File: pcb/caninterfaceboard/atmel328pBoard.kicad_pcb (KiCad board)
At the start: 2 copper layers, 97.2 x 50.5 mm, 74 parts, among them J1 UART, J10 NTC2, J12 Flywheel, J13 1Wire, J2 NMEA2000, J3 AVR ISP, J4 NTC3, J5 NTC4, J6 FuelLevel, J7 Engine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

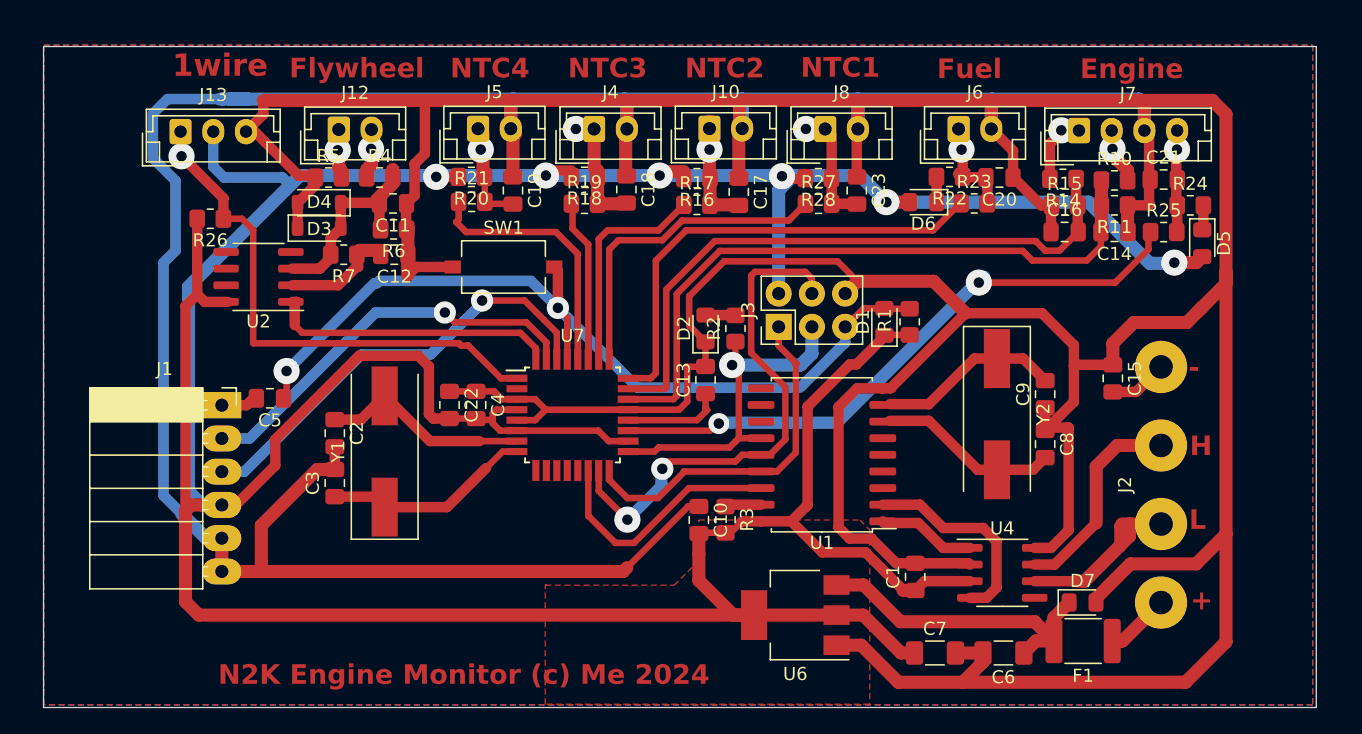
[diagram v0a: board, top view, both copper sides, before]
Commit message: Added oil pressure and status, modified pcb
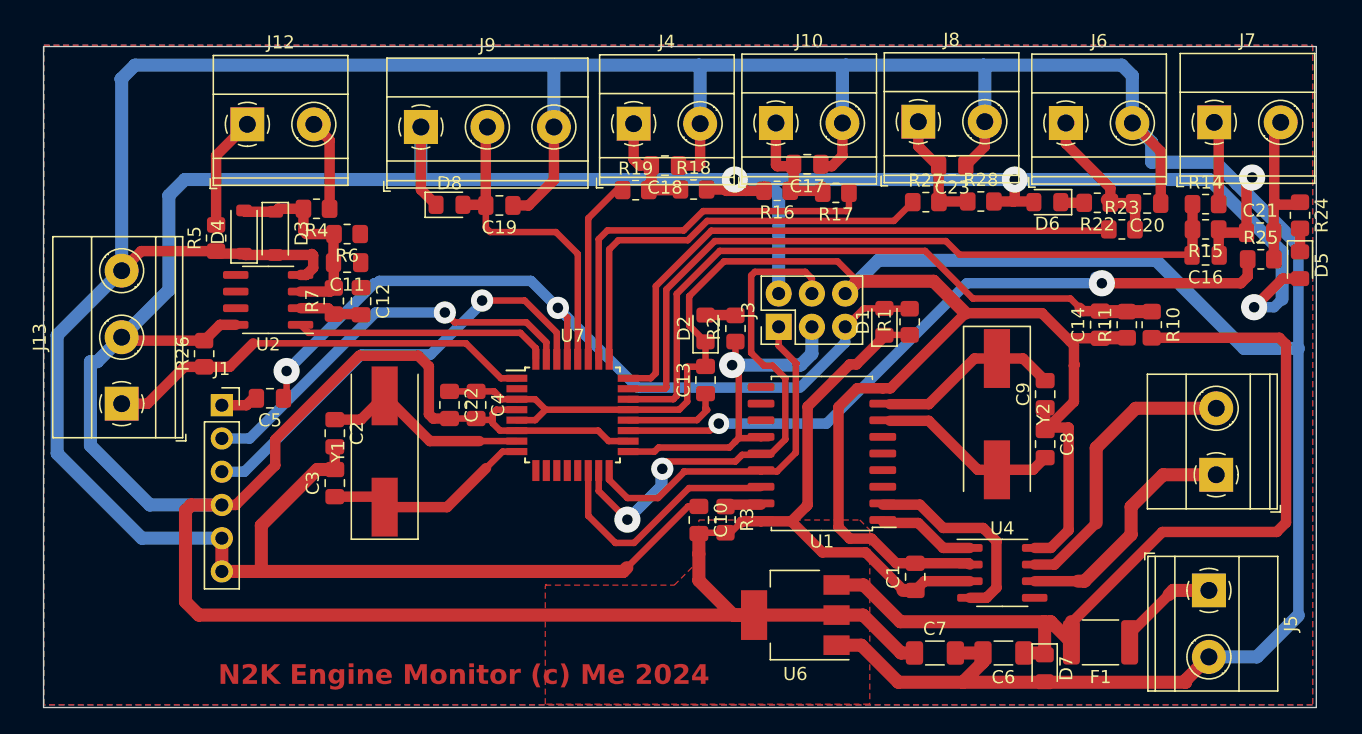
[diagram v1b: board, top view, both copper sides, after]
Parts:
- removed C15: 1uF, Capacitor_SMD:C_0805_2012Metric_Pad1.18x1.45mm_HandSolder
- removed R20: 4.7K, Resistor_SMD:R_0805_2012Metric_Pad1.20x1.40mm_HandSolder
- removed R21: 100K, Resistor_SMD:R_0805_2012Metric_Pad1.20x1.40mm_HandSolder
- removed SW1: Reset, Button_Switch_SMD:SW_Tactile_SPST_NO_Straight_CK_PTS636Sx25SMTRLFS
- added D8: S1J, Diode_SMD:D_0805_2012Metric_Pad1.15x1.40mm_HandSolder, F.Cu at (138.7, 62.7)
- added J9: Oil Pressure, TerminalBlock_Phoenix:TerminalBlock_Phoenix_MKDS-1,5-3-5.08_1x03_P5.08mm_Horizontal, F.Cu at (136.5, 56.7)
- J1: footprint Connector_PinSocket_2.54mm:PinSocket_1x06_P2.54mm_Horizontal -> Connector_PinSocket_2.54mm:PinSocket_1x06_P2.54mm_Vertical
- J10, J12, J4, J6, J8: footprint Connector_JST:JST_EH_B2B-EH-A_1x02_P2.50mm_Vertical -> TerminalBlock_Phoenix:TerminalBlock_Phoenix_MKDS-1,5-2-5.08_1x02_P5.08mm_Horizontal
- J13: footprint Connector_JST:JST_EH_B3B-EH-A_1x03_P2.50mm_Vertical -> TerminalBlock_Phoenix:TerminalBlock_Phoenix_MKDS-1,5-3-5.08_1x03_P5.08mm_Horizontal
- J2: value NMEA2000 -> CAN; footprint Connector_Wire:SolderWire-1.5sqmm_1x04_P6mm_D1.7mm_OD3mm -> TerminalBlock_Phoenix:TerminalBlock_Phoenix_MKDS-1,5-2-5.08_1x02_P5.08mm_Horizontal
- J5: value NTC4 -> 12V In; footprint Connector_JST:JST_EH_B2B-EH-A_1x02_P2.50mm_Vertical -> TerminalBlock_Phoenix:TerminalBlock_Phoenix_MKDS-1,5-2-5.08_1x02_P5.08mm_Horizontal
- J7: footprint Connector_JST:JST_EH_B4B-EH-A_1x04_P2.50mm_Vertical -> TerminalBlock_Phoenix:TerminalBlock_Phoenix_MKDS-1,5-2-5.08_1x02_P5.08mm_Horizontal
- moved J5 66.0 mm to (196.7, 92.1), turned to -90 degrees
- moved J13 21.3 mm to (113.6, 77.9), turned to 90 degrees
- moved R28 12.5 mm to (179.3, 62.4), turned to 0 degrees
- moved R23 11.5 mm to (190.0, 64.6)
- moved C20 11.5 mm to (192.0, 62.6)
- moved R22 11.5 mm to (188.2, 62.5)
- moved R10 11.4 mm to (192.3, 71.8), turned to -90 degrees
- moved R14 11.1 mm to (196.4, 62.6), turned to 0 degrees
- moved R15 10.9 mm to (196.4, 64.6), turned to 180 degrees
- moved C16 10.9 mm to (196.4, 66.5), turned to 180 degrees
- moved R17 10.7 mm to (168.2, 61.8), turned to 180 degrees
- moved J2 10.6 mm to (197.3, 83.3)
- moved J7 10.4 mm to (197.1, 56.4)
- moved R26 10.3 mm to (119.9, 74.1), turned to 90 degrees
- moved R5 9.75 mm to (120.9, 65.2), turned to 90 degrees
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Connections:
- C19 pad 2: Net-(J5-Pin_1) -> A5
- C6 pad 1: Net-(D7-K) -> Engine Batt+
- D7 pad 1: Net-(D7-K) -> Engine Batt+
- F1 pad 2: Net-(D7-K) -> Engine Batt+
- J2 pad 1: 12V -> CANHL
- J2 pad 2: CANHL -> CANH
- J5 pad 1: Net-(J5-Pin_1) -> 12V
- J7 pad 2: Engine Batt+ -> Coolant
- U6 pad 3: Net-(D7-K) -> Engine Batt+
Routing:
- net Engine Batt+: track 5.63 -> 70.7 mm, vias 1 -> 0
- net Engine Block: track 563.3 -> 508.9 mm, vias 0 -> 1
- net Net-(D7-K): track 24.5 -> 0.00 mm
- net A6: track 72.2 -> 54.4 mm
- net 5V: track 320.8 -> 337.0 mm, vias 6 -> 3
- net A3: track 16.8 -> 30.9 mm
- net Net-(J5-Pin_1): track 9.46 -> 0.00 mm, vias 1 -> 0
- net A1: track 36.1 -> 45.3 mm
- net A2: track 24.8 -> 33.1 mm
- net A0: track 48.5 -> 56.5 mm
- net D3: track 40.6 -> 33.2 mm, vias 1 -> 0
- net CANH: track 15.9 -> 22.2 mm
- net A5: track 20.0 -> 25.7 mm
- net Net-(J12-Pin_1): track 4.86 -> 9.34 mm, vias 1 -> 0
- net Net-(J2-Pin_4): track 4.47 -> 0.00 mm
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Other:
- board text removed: "+"
- board text removed: "-"
- board text removed: "1wire"
- board text removed: "Engine"
- board text removed: "Flywheel"
- board text removed: "Fuel"
- board text removed: "H"
- board text removed: "L"
- board text removed: "NTC1"
- board text removed: "NTC2"
- board text removed: "NTC3"
- board text removed: "NTC4"

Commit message: Finally mare the RPM to pulse amp stable
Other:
- board text added: "Alternator B+"
- board text added: "Alternator NTC"
- board text added: "CanH"
- board text added: "CanL"
- board text added: "Coolant + Powered by 12V"
- board text added: "Engine Block"
- board text added: "Engine Room NTC"
- board text added: "Engine Switched 12V"
- board text added: "Exhaust NTC"
- board text added: "Flywheel +"
- board text added: "Flywheel -"
- board text added: "FuelLevel +"
- board text added: "FuelLevel 0v"
- board text added: "ISP 5v MOSI 0v MISO SCK ISP_RST"
- board text added: "NTC 0v"
- board text added: "Oil Pressure 0v"
- board text added: "Oil Pressure 5v"
- board text added: "Oil Pressure Signal"
- board text added: "One Wire 0v"
- board text added: "One Wire 5V"
- board text added: "One Wire Signal"
- board text added: "Uart 5V"
- board text added: "Uart DTR"
- board text added: "Uart GND"
- board text added: "Uart RX"
- board text added: "Uart TX"
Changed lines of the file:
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@@
+    (effects (font (size 1.5 1.5) (thickness 0.3) bold) (justify left bottom))
+  )
+  (gr_text "Uart GND" (at 84.4804 100.838) (layer "Dwgs.User")
+    (effects (font (size 1.5 1.5) (thickness 0.3) bold) (justify left bottom))
+  )
+  (gr_text "Uart RX" (at 84.7852 89.8652) (layer "Dwgs.User")
+    (effects (font (size 1.5 1.5) (thickness 0.3) bold) (justify left bottom))
+  )
+  (gr_text "ISP\n5v    MOSI  0v\nMISO  SCK   ISP_RST" (at 163.2204 113.03) (layer "Dwgs.User")
+    (effects (font (size 1.5 1.5) (thickness 0.3) bold) (justify left bottom))
+  )
+  (gr_text "Flywheel -" (at 123.698 49.7332 90) (layer "Dwgs.User")
+    (effects (font (size 1.5 1.5) (thickness 0.3) bold) (justify left bottom))
+  )
+  (gr_text "FuelLevel +" (at 186.5884 49.8856 90) (layer "Dwgs.User")
+    (effects (font (size 1.5 1.5) (thickness 0.3) bold) (justify left bottom))
+  )
+  (gr_text "Uart GND" (at 84.4804 98.3488) (layer "Dwgs.User")
+    (effects (font (size 1.5 1.5) (thickness 0.3) bold) (justify left bottom))
+  )
+  (gr_text "Flywheel +" (at 129.1844 49.9364 90) (layer "Dwgs.User")
+    (effects (font (size 1.5 1.5) (thickness 0.3) bold) (justify left bottom))
+  )
+  (gr_text "Exhaust NTC" (at 175.514 49.3268 90) (layer "Dwgs.User")
+    (effects (font (size 1.5 1.5) (thickness 0.3) bold) (justify left bottom))
+  )
+  (gr_text "Engine Block" (at 207.01 97.7392) (layer "Dwgs.User")
+    (effects (font (size 1.5 1.5) (thickness 0.3) bold) (justify left bottom))
+  )
+  (gr_text "One Wire 0v" (at 92.2528 68.072) (layer "Dwgs.User")
+    (effects (font (size 1.5 1.5) (thickness 0.3) bold) (justify left bottom))
+  )
+  (gr_text "NTC 0v" (at 180.4924 49.5808 90) (layer "Dwgs.User")
+    (effects (font (size 1.5 1.5) (thickness 0.3) bold) (justify left bottom))
+  )
+  (gr_text "Alternator B+" (at 198.0692 49.53 90) (layer "Dwgs.User")
+    (effects (font (size 1.5 1.5) (thickness 0.3) bold) (justify left bottom))
+  )
+  (gr_text "Oil Pressure 0v" (at 147.3708 49.5808 90) (layer "Dwgs.User")
+    (effects (font (size 1.5 1.5) (thickness 0.3) bold) (justify left bottom))
+  )
+  (gr_text "Alternator NTC" (at 164.1348 49.4284 90) (layer "Dwgs.User")
+    (effects (font (size 1.5 1.5) (thickness 0.3) bold) (justify left bottom))
+  )
+  (gr_text "CanH" (at 207.4672 80.01) (layer "Dwgs.User")
+    (effects (font (size 1.5 1.5) (thickness 0.3) bold) (justify left bottom))
+  )
+  (gr_text "Uart 5V" (at 84.6836 95.3516) (layer "Dwgs.User")
+    (effects (font (size 1.5 1.5) (thickness 0.3) bold) (justify left bottom))
+  )
+  (gr_text "Engine Switched 12V" (at 207.2132 92.5576) (layer "Dwgs.User")
+    (effects (font (size 1.5 1.5) (thickness 0.3) bold) (justify left bottom))
+  )
+  (gr_text "Coolant +\nPowered by 12V" (at 205.9432 49.5808 90) (layer "Dwgs.User")
+    (effects (font (size 1.5 1.5) (thickness 0.3) bold) (justify left bottom))
+  )
+  (gr_text "CanL" (at 207.8736 83.9724) (layer "Dwgs.User")
+    (effects (font (size 1.5 1.5) (thickness 0.3) bold) (justify left bottom))
+  )
+  (gr_text "One Wire Signal" (at 93.218 79.2988) (layer "Dwgs.User")
+    (effects (font (size 1.5 1.5) (thickness 0.3) bold) (justify left bottom))
+  )
+  (gr_text "FuelLevel 0v" (at 191.4144 49.8856 90) (layer "Dwgs.User")
+    (effects (font (size 1.5 1.5) (thickness 0.3) bold) (justify left bottom))
+  )
+  (gr_text "Oil Pressure 5v" (at 137.2108 49.6316 90) (layer "Dwgs.User")
+    (effects (font (size 1.5 1.5) (thickness 0.3) bold) (justify left bottom))
+  )
+  (gr_text "NTC 0v" (at 169.5196 49.0728 90) (layer "Dwgs.User")
+    (effects (font (size 1.5 1.5) (thickness 0.3) bold) (justify left bottom))
+  )
+  (gr_text "Oil Pressure Signal" (at 142.4432 49.3268 90) (layer "Dwgs.User")
+    (effects (font (size 1.5 1.5) (thickness 0.3) bold) (justify left bottom))
+  )
+  (gr_text "Uart TX" (at 84.582 92.7608) (layer "Dwgs.User")
+    (effects (font (size 1.5 1.5) (thickness 0.3) bold) (justify left bottom))
+  )
+  (gr_text "Engine Room NTC" (at 153.6192 49.2252 90) (layer "Dwgs.User")
+    (effects (font (size 1.5 1.5) (thickness 0.3) bold) (justify left bottom))
+  )
+  (gr_text "NTC 0v" (at 158.496 49.276 90) (layer "Dwgs.User")
+    (effects (font (size 1.5 1.5) (thickness 0.3) bold) (justify left bottom))
+  )
+  (gr_text "One Wire 5V" (at 92.6084 73.7108) (layer "Dwgs.User")
+    (effects (font (size 1.5 1.5) (thickness 0.3) bold) (justify left bottom))
+  )
+  (gr_text "Uart DTR" (at 84.6328 87.3252) (layer "Dwgs.User")
     (effects (font (size 1.5 1.5) (thickness 0.3) bold) (justify left bottom))
   )
